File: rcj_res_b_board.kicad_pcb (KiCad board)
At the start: 2 copper layers, 90 x 100 mm, 97 parts, among them P1 CONN_01X02, P10 PING0, P11 MPU9250, P12 SERVO0, P13 CONN_01X04, P14 CONN_01X03, P15 CONN_01X03, P16 CONN_01X04, P17 CONN_01X04, P18 CONN_01X04, P19 CONN_01X04, P2 CONN_01X02, P3 GP2Y0A41SK0F, P4 GP2Y0A41SK0F, P5 GP2Y0A41SK0F, P6 GP2Y0A41SK0F, P7 GP2Y0A21YK, P8 GP2Y0A21YK, P9 GP2Y0A21YK, SW1 SW_PUSH, SW2 SW_PUSH, SW3 SWITCH_INV, U1 OPB733TR

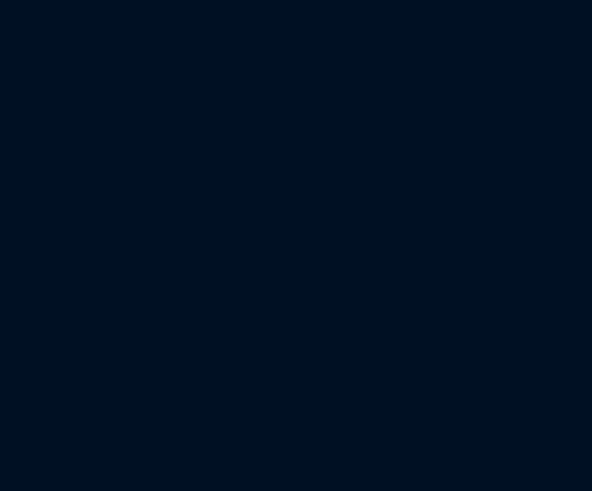
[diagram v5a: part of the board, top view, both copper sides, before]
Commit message: Changed power supply
Now using one 3.3V ULDO regulator
Removed 5V power (ping powered directly from battery)
Added filtering network (chokes and caps)
Added 2 indicator LEDs
Fixed EVQPL* button footprints
Added pcbnew lib table
Updated .gitignore to ignore other unneccesary files (_saved*)
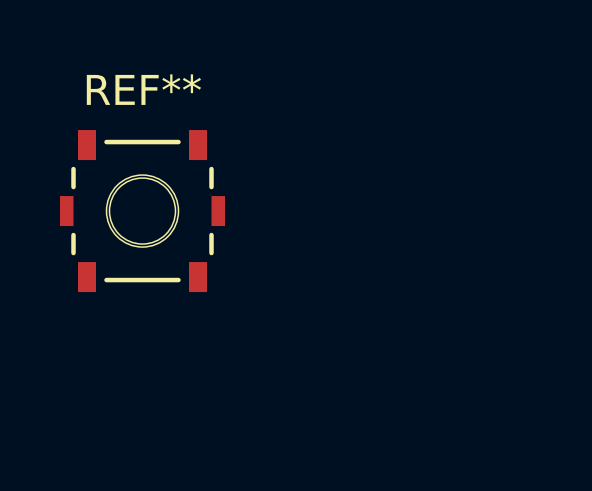
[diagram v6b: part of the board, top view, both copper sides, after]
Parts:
- added REF**: EVQPL, EVQPL, F.Cu at (0.00, 0.00)
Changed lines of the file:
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@@
-(kicad_pcb (version 4) (host pcbnew 0.201512201246+6385~39~ubuntu15.04.1-stable)
+(kicad_pcb (version 4) (host pcbnew 0.201512231247+6403~40~ubuntu15.04.1-stable)
   (general
     (links 228)
-    (no_connects 156)
+    (no_connects 158)
     (area 19.924999 49.924999 110.075001 150.100001)
     (thickness 1.6)
@@
     (tracks 101)
     (zones 0)
-    (modules 97)
+    (modules 98)
     (nets 98)
   )
@@
     (add_net "Net-(MD1-Pad7)")
   )
+  (module EVQPL (layer F.Cu)
+    (at 0 0)
+    (fp_text reference REF** (at 0 -4) (layer F.SilkS)
+      (effects (font (size 1 1) (thickness 0.15)))
+    )
+    (fp_text value EVQPL (at 0 4) (layer F.Fab)
+      (effects (font (size 1 1) (thickness 0.15)))
+    )
+    (fp_line (start 2.3 -0.8) (end 2.3 -1.4) (layer F.SilkS) (width 0.15))
+    (fp_line (start 2.3 1.4) (end 2.3 0.8) (layer F.SilkS) (width 0.15))
+    (fp_line (start -1.2 2.3) (end 1.2 2.3) (layer F.SilkS) (width 0.15))
+    (fp_line (start -2.3 0.8) (end -2.3 1.4) (layer F.SilkS) (width 0.15))
+    (fp_line (start -2.3 -1.4) (end -2.3 -0.8) (layer F.SilkS) (width 0.15))
+    (fp_line (start -1.2 -2.3) (end 1.2 -2.3) (layer F.SilkS) (width 0.15))
+    (fp_circle (center 0 0) (end 0 -1.2) (layer F.SilkS) (width 0.05))
+    (fp_circle (center 0 0) (end 0 -1.1) (layer F.SilkS) (width 0.05))
+    (pad 1 smd rect (at -1.85 -2.2) (size 0.6 1) (layers F.Cu F.Paste F.Mask))
+    (pad 1 smd rect (at 1.85 -2.2) (size 0.6 1) (layers F.Cu F.Paste F.Mask))
+    (pad 2 smd rect (at -1.85 2.2) (size 0.6 1) (layers F.Cu F.Paste F.Mask))
+    (pad 2 smd rect (at 1.85 2.2) (size 0.6 1) (layers F.Cu F.Paste F.Mask))
+    (pad "" smd rect (at -2.525 0) (size 0.45 1) (layers F.Cu F.Paste F.Mask))
+    (pad "" smd rect (at 2.525 0) (size 0.45 1) (layers F.Cu F.Paste F.Mask))
+  )
   (module Connect:1pin (layer F.Cu)
     (at 104 147.5)
@@
       (net 6 GNDA))
   )
-  (module Custom:EVQPL (layer F.Cu)
-    (at 42 74)
-    (fp_text reference SW1 (at 0 -4) (layer F.SilkS)
-      (effects (font (size 1 1) (thickness 0.15)))
-    )
-    (fp_text value SW_PUSH (at 0 4) (layer F.Fab)
-      (effects (font (size 1 1) (thickness 0.15)))
-    )
-    (fp_line (start 2.3 -0.8) (end 2.3 -1.4) (layer F.SilkS) (width 0.15))
-    (fp_line (start 2.3 1.4) (end 2.3 0.8) (layer F.SilkS) (width 0.15))
-    (fp_line (start -1.2 2.3) (end 1.2 2.3) (layer F.SilkS) (width 0.15))
-    (fp_line (start -2.3 0.8) (end -2.3 1.4) (layer F.SilkS) (width 0.15))
-    (fp_line (start -2.3 -1.4) (end -2.3 -0.8) (layer F.SilkS) (width 0.15))
-    (fp_line (start -1.2 -2.3) (end 1.2 -2.3) (layer F.SilkS) (width 0.15))
-    (fp_circle (center 0 0) (end 0 -1.2) (layer F.SilkS) (width 0.05))
-    (fp_circle (center 0 0) (end 0 -1.1) (layer F.SilkS) (width 0.05))
-    (pad 1 smd rect (at -1.85 -2.2) (size 0.6 1) (layers F.Cu F.Paste F.Mask)
-      (net 78 /USR1))
-    (pad 2 smd rect (at 1.85 -2.2) (size 0.6 1) (layers F.Cu F.Paste F.Mask)
-      (net 2 GNDD))
-    (pad 1 smd rect (at -1.85 2.2) (size 0.6 1) (layers F.Cu F.Paste F.Mask)
-      (net 78 /USR1))
-    (pad 2 smd rect (at 1.85 2.2) (size 0.6 1) (layers F.Cu F.Paste F.Mask)
-      (net 2 GNDD))
-    (pad "" smd rect (at -2.525 0) (size 0.45 1) (layers F.Cu F.Paste F.Mask))
-    (pad "" smd rect (at 2.525 0) (size 0.45 1) (layers F.Cu F.Paste F.Mask))
-  )
-  (module Custom:EVQPL (layer F.Cu)
-    (at 88 74)
-    (fp_text reference SW2 (at 0 -4) (layer F.SilkS)
-      (effects (font (size 1 1) (thickness 0.15)))
-    )
-    (fp_text value SW_PUSH (at 0 4) (layer F.Fab)
-      (effects (font (size 1 1) (thickness 0.15)))
-    )
-    (fp_line (start 2.3 -0.8) (end 2.3 -1.4) (layer F.SilkS) (width 0.15))
-    (fp_line (start 2.3 1.4) (end 2.3 0.8) (layer F.SilkS) (width 0.15))
-    (fp_line (start -1.2 2.3) (end 1.2 2.3) (layer F.SilkS) (width 0.15))
-    (fp_line (start -2.3 0.8) (end -2.3 1.4) (layer F.SilkS) (width 0.15))
-    (fp_line (start -2.3 -1.4) (end -2.3 -0.8) (layer F.SilkS) (width 0.15))
-    (fp_line (start -1.2 -2.3) (end 1.2 -2.3) (layer F.SilkS) (width 0.15))
-    (fp_circle (center 0 0) (end 0 -1.2) (layer F.SilkS) (width 0.05))
-    (fp_circle (center 0 0) (end 0 -1.1) (layer F.SilkS) (width 0.05))
-    (pad 1 smd rect (at -1.85 -2.2) (size 0.6 1) (layers F.Cu F.Paste F.Mask)
-      (net 79 /USR2))
-    (pad 2 smd rect (at 1.85 -2.2) (size 0.6 1) (layers F.Cu F.Paste F.Mask)
-      (net 2 GNDD))
-    (pad 1 smd rect (at -1.85 2.2) (size 0.6 1) (layers F.Cu F.Paste F.Mask)
-      (net 79 /USR2))
-    (pad 2 smd rect (at 1.85 2.2) (size 0.6 1) (layers F.Cu F.Paste F.Mask)
-      (net 2 GNDD))
-    (pad "" smd rect (at -2.525 0) (size 0.45 1) (layers F.Cu F.Paste F.Mask))
-    (pad "" smd rect (at 2.525 0) (size 0.45 1) (layers F.Cu F.Paste F.Mask))
-  )
   (module Custom:JS202011SCQN (layer F.Cu)
     (at 55 71 90)
@@
     )
   )
+  (module Custom:EVQPL (layer F.Cu)
+    (at 42 74)
+    (fp_text reference SW1 (at 0 -4) (layer F.SilkS)
+      (effects (font (size 1 1) (thickness 0.15)))
+    )
+    (fp_text value SW_PUSH (at 0 4) (layer F.Fab)
+      (effects (font (size 1 1) (thickness 0.15)))
+    )
+    (fp_line (start 2.3 -0.8) (end 2.3 -1.4) (layer F.SilkS) (width 0.15))
+    (fp_line (start 2.3 1.4) (end 2.3 0.8) (layer F.SilkS) (width 0.15))
+    (fp_line (start -1.2 2.3) (end 1.2 2.3) (layer F.SilkS) (width 0.15))
+    (fp_line (start -2.3 0.8) (end -2.3 1.4) (layer F.SilkS) (width 0.15))
+    (fp_line (start -2.3 -1.4) (end -2.3 -0.8) (layer F.SilkS) (width 0.15))
+    (fp_line (start -1.2 -2.3) (end 1.2 -2.3) (layer F.SilkS) (width 0.15))
+    (fp_circle (center 0 0) (end 0 -1.2) (layer F.SilkS) (width 0.05))
+    (fp_circle (center 0 0) (end 0 -1.1) (layer F.SilkS) (width 0.05))
+    (pad 1 smd rect (at -1.85 -2.2) (size 0.6 1) (layers F.Cu F.Paste F.Mask)
+      (net 78 /USR1))
+    (pad 1 smd rect (at 1.85 -2.2) (size 0.6 1) (layers F.Cu F.Paste F.Mask)
+      (net 78 /USR1))
+    (pad 2 smd rect (at -1.85 2.2) (size 0.6 1) (layers F.Cu F.Paste F.Mask)
+      (net 2 GNDD))
+    (pad 2 smd rect (at 1.85 2.2) (size 0.6 1) (layers F.Cu F.Paste F.Mask)
+      (net 2 GNDD))
+    (pad "" smd rect (at -2.525 0) (size 0.45 1) (layers F.Cu F.Paste F.Mask))
+    (pad "" smd rect (at 2.525 0) (size 0.45 1) (layers F.Cu F.Paste F.Mask))
+  )
+  (module Custom:EVQPL (layer F.Cu)
+    (at 88 74)
+    (fp_text reference SW2 (at 0 -4) (layer F.SilkS)
+      (effects (font (size 1 1) (thickness 0.15)))
+    )
+    (fp_text value SW_PUSH (at 0 4) (layer F.Fab)
+      (effects (font (size 1 1) (thickness 0.15)))
+    )
+    (fp_line (start 2.3 -0.8) (end 2.3 -1.4) (layer F.SilkS) (width 0.15))
+    (fp_line (start 2.3 1.4) (end 2.3 0.8) (layer F.SilkS) (width 0.15))
+    (fp_line (start -1.2 2.3) (end 1.2 2.3) (layer F.SilkS) (width 0.15))
+    (fp_line (start -2.3 0.8) (end -2.3 1.4) (layer F.SilkS) (width 0.15))
+    (fp_line (start -2.3 -1.4) (end -2.3 -0.8) (layer F.SilkS) (width 0.15))
+    (fp_line (start -1.2 -2.3) (end 1.2 -2.3) (layer F.SilkS) (width 0.15))
+    (fp_circle (center 0 0) (end 0 -1.2) (layer F.SilkS) (width 0.05))
+    (fp_circle (center 0 0) (end 0 -1.1) (layer F.SilkS) (width 0.05))
+    (pad 1 smd rect (at -1.85 -2.2) (size 0.6 1) (layers F.Cu F.Paste F.Mask)
+      (net 79 /USR2))
+    (pad 1 smd rect (at 1.85 -2.2) (size 0.6 1) (layers F.Cu F.Paste F.Mask)
+      (net 79 /USR2))
+    (pad 2 smd rect (at -1.85 2.2) (size 0.6 1) (layers F.Cu F.Paste F.Mask)
+      (net 2 GNDD))
+    (pad 2 smd rect (at 1.85 2.2) (size 0.6 1) (layers F.Cu F.Paste F.Mask)
+      (net 2 GNDD))
+    (pad "" smd rect (at -2.525 0) (size 0.45 1) (layers F.Cu F.Paste F.Mask))
+    (pad "" smd rect (at 2.525 0) (size 0.45 1) (layers F.Cu F.Paste F.Mask))
+  )
   (gr_text - (at 79.54 69.46) (layer B.SilkS)

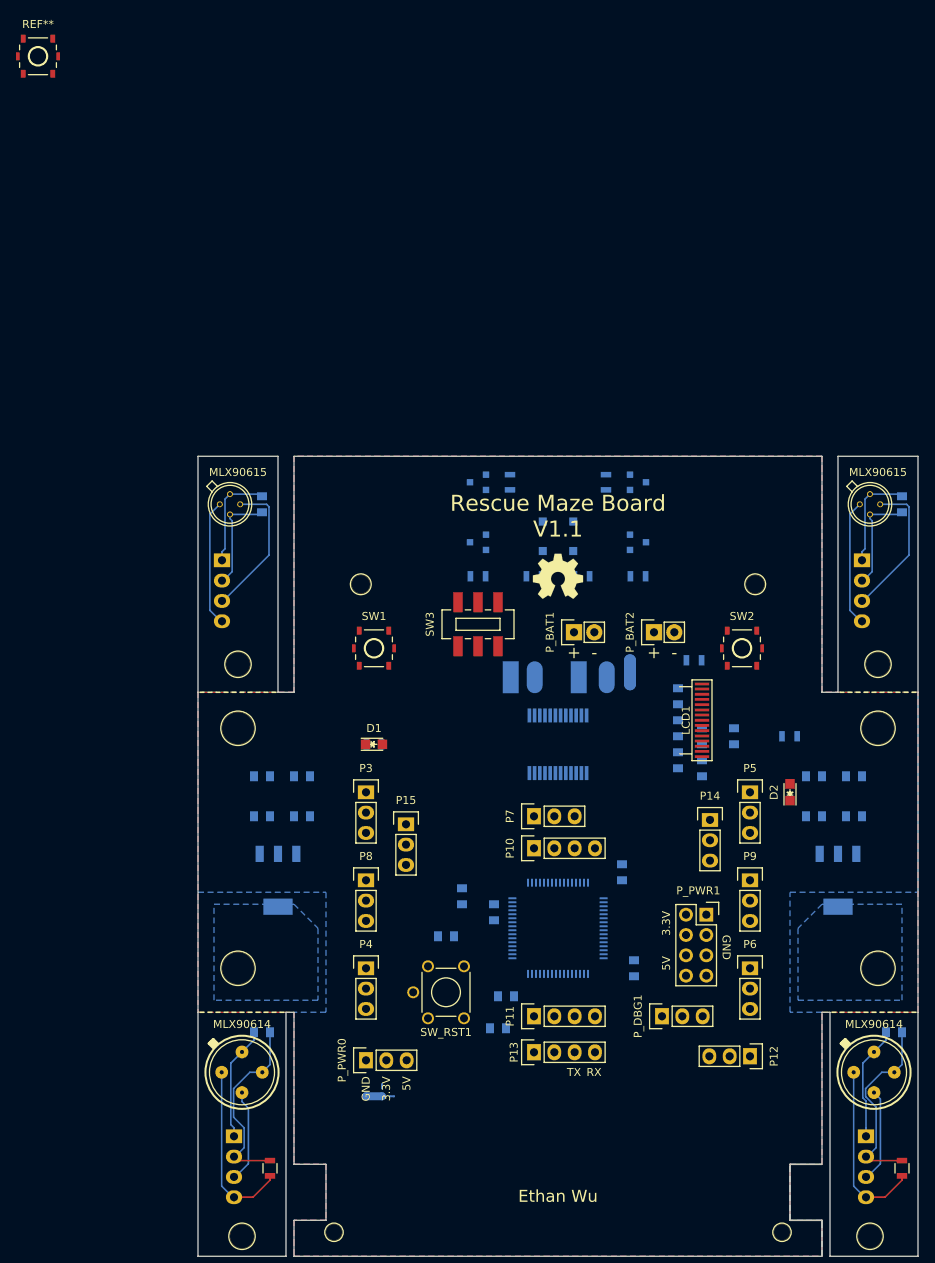
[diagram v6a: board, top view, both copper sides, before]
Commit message: Preliminary layout
Changed push-button footprints
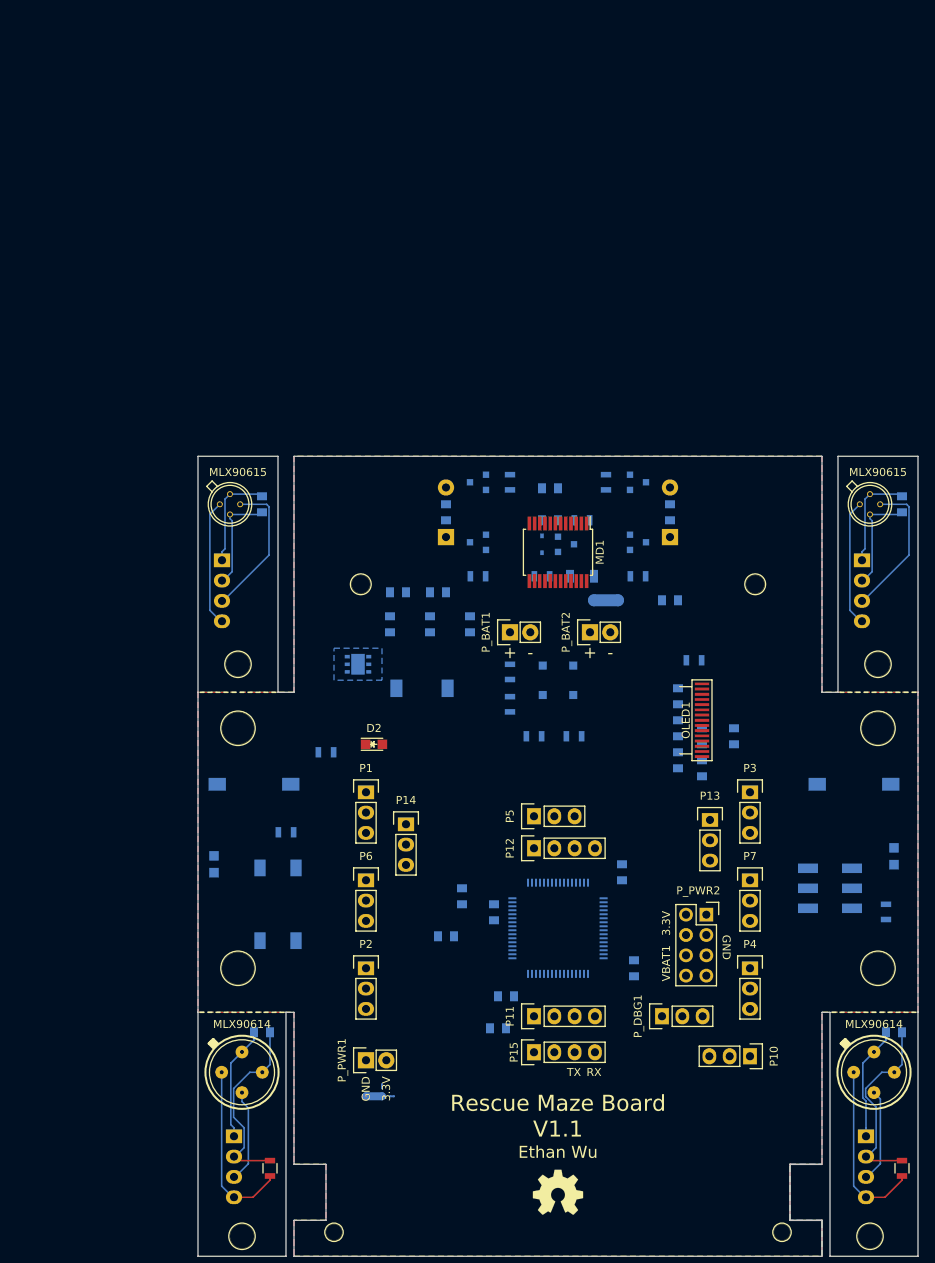
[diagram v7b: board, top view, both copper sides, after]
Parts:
- removed the C7 at (102.0, 90.0)
- removed the C8 at (97.0, 90.0)
- removed the D2 at (94.0, 92.0)
- removed P_PWR0: CONN_01X03, Socket_Strips:Socket_Strip_Straight_1x03
- removed the R2 at (94.0, 85.0)
- removed REF**: EVQPL, EVQPL
- removed REG2: LD1117S50TR, TO_SOT_Packages_SMD:SOT-223
- added C1: 3.3nF, Capacitors_SMD:C_0805, B.Cu at (79.0, 57.0)
- added C10: 0.1uF, Capacitors_SMD:C_0805, B.Cu at (45.0, 67.0)
- added C14: 1uF, Capacitors_SMD:C_0805, B.Cu at (50.0, 67.0)
- added C2: 3.3nF, Capacitors_SMD:C_0805, B.Cu at (51.0, 57.0)
- added D1: 6.8V, Diodes_SMD:SOD-323, B.Cu at (63.0, 61.0)
- added D3: LED, LEDs:LED-0805, B.Cu at (107.0, 100.0)
- added D4: LED, LEDs:LED-0805, B.Cu at (22.0, 101.0)
- added L1: L_Small, Capacitors_SMD:C_0805, B.Cu at (54.0, 71.0)
- added L2: L_Small, Choke_SMD:Choke_SMD_7.3x7.3_H3.5, B.Cu at (48.0, 79.0)
- added P_PWR1: CONN_01X02, Socket_Strips:Socket_Strip_Straight_1x02, F.Cu at (41.0, 125.5)
- added Q1: Q_PMOS_GSD, TO_SOT_Packages_SMD:SOT-23, B.Cu at (66.0, 61.0)
- added R13: 1k, Resistors_SMD:R_0805, B.Cu at (106.0, 107.0)
- added R14: 1k, Resistors_SMD:R_0805, B.Cu at (31.0, 97.0)
- added R5: 100k, Resistors_SMD:R_0805, B.Cu at (63.0, 65.0)
- added R6: 1, Resistors_SMD:R_0805, B.Cu at (68.0, 58.0)
- added R7: 10k, Resistors_SMD:R_0805, B.Cu at (62.0, 85.0)
- added R8: 10k, Resistors_SMD:R_0805, B.Cu at (67.0, 85.0)
- C3: value 0.1uF -> 10uF; footprint Capacitors_SMD:C_0805 -> Capacitors_SMD:C_1206
- C5: value 10uF -> 0.47uF
- C6: value 10uF -> 0.1uF
- MD1: moved to F.Cu
- REG1: value LD1117S33TR -> LD39200PU; footprint TO_SOT_Packages_SMD:SOT-223 -> Housings_DFN_QFN:DFN-6-1EP_3x3mm_Pitch0.95mm
- SW1, SW2: footprint Custom:EVQPL -> Buttons_Switches_SMD:SW_SPST_FSMSM; moved to B.Cu
- SW3: moved to B.Cu
- SW_RST1: footprint Custom:EVQPB -> Custom:Switch_FSM_JSM; moved to B.Cu
- moved G001 77.0 mm to (65.0, 142.0)
- moved C5 55.9 mm to (64.0, 54.0)
- moved SW3 55.0 mm to (99.0, 104.0), turned to 0 degrees
- moved C4 48.2 mm to (64.0, 58.0), turned to 180 degrees
- moved C3 43.0 mm to (68.0, 65.0), turned to 0 degrees
- moved C6 32.4 mm to (79.0, 68.0), turned to 180 degrees
- moved C15 28.8 mm to (49.0, 71.0), turned to 90 degrees
- moved C16 28.8 mm to (44.0, 71.0), turned to 270 degrees
- moved REG1 28.8 mm to (40.0, 76.0)
- moved P8 26.5 mm to (79.0, 60.1), turned to 90 degrees
- moved P9 24.1 mm to (51.0, 60.1), turned to 90 degrees
- moved MD1 24.0 mm to (65.0, 62.0)
- moved SW_RST1 23.7 mm to (30.0, 106.0)
- moved SW1 22.7 mm to (27.0, 91.0), turned to 180 degrees
- moved SW2 22.0 mm to (102.0, 91.0)
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- renumbered C19 to C11, C20 to C12, C21 to C13, C1 to C15, C2 to C16, C13 to C17, C12 to C18, C10 to C19, C11 to C20, C15 to C21, C9 to C22, C14 to C23, C16 to C7, C17 to C8, C18 to C9, D1 to D2, LCD1 to OLED1, P3 to P1, P12 to P10, P10 to P12, P14 to P13, P15 to P14, P13 to P15, P4 to P2, P5 to P3, P6 to P4, P7 to P5, P8 to P6, P9 to P7, P1 to P8, P2 to P9, P_PWR1 to P_PWR2, R3 to R1, R9 to R10, R8 to R11, R1 to R12, R5 to R2, R4 to R3, R6 to R4, R7 to R9
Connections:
- net /USR1 renamed /SW_USR1
- net /USR2 renamed /SW_USR2
- C15 pad 1: VCC -> /VBAT1
- C3 pad 1: VCC -> Net-(C3-Pad1)
- C3 pad 2: GNDD -> GNDPWR
- C4 pad 1: /3.3V -> Net-(C4-Pad1)
- C4 pad 2: GNDD -> GNDPWR
- C5 pad 1: VCC -> Net-(C4-Pad1)
- C5 pad 2: GNDD -> GNDPWR
- C6 pad 1: /5V -> GNDD
- C6 pad 2: GNDD -> /3.3V
- MCU1 pad 25: Net-(MCU1-Pad25) -> /VBAT_MON
- MCU1 pad 3: Net-(MCU1-Pad3) -> /LED_USR1
- MCU1 pad 4: Net-(MCU1-Pad4) -> /LED_USR2
- MD1 pad 13: VCC -> Net-(C4-Pad1)
- MD1 pad 14: VCC -> Net-(C4-Pad1)
- MD1 pad 24: VCC -> Net-(C4-Pad1)
- P1 pad 1: /5V -> /3.3V
- P10 pad 2: /5V -> /3.3V
- P11 pad 1: /5V -> /3.3V
- P12 pad 1: /5V -> /VBAT1
- P2 pad 1: /5V -> /3.3V
- P3 pad 1: /5V -> /3.3V
- P4 pad 1: /5V -> /3.3V
- P5 pad 1: /5V -> /3.3V
- P6 pad 1: /5V -> /3.3V
- P7 pad 1: /5V -> /3.3V
- P_PWR2 pad 6: /5V -> /VBAT1
- P_PWR2 pad 8: /5V -> /VBAT1
- REG1 pad 1: GNDD -> /3.3V
- REG1 pad 3: VCC -> GNDD
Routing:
- removed copper zone on B.Cu, net Net-(REG1-Pad4)
- removed copper zone on B.Cu, net Net-(REG2-Pad4)
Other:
- board text added: "VBAT1"
- board text removed: "5V"
